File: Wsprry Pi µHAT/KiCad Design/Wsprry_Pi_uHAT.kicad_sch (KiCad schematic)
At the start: 9 parts, among them J1 GPIO, SW1 SW_Push, U2 CAT24C32

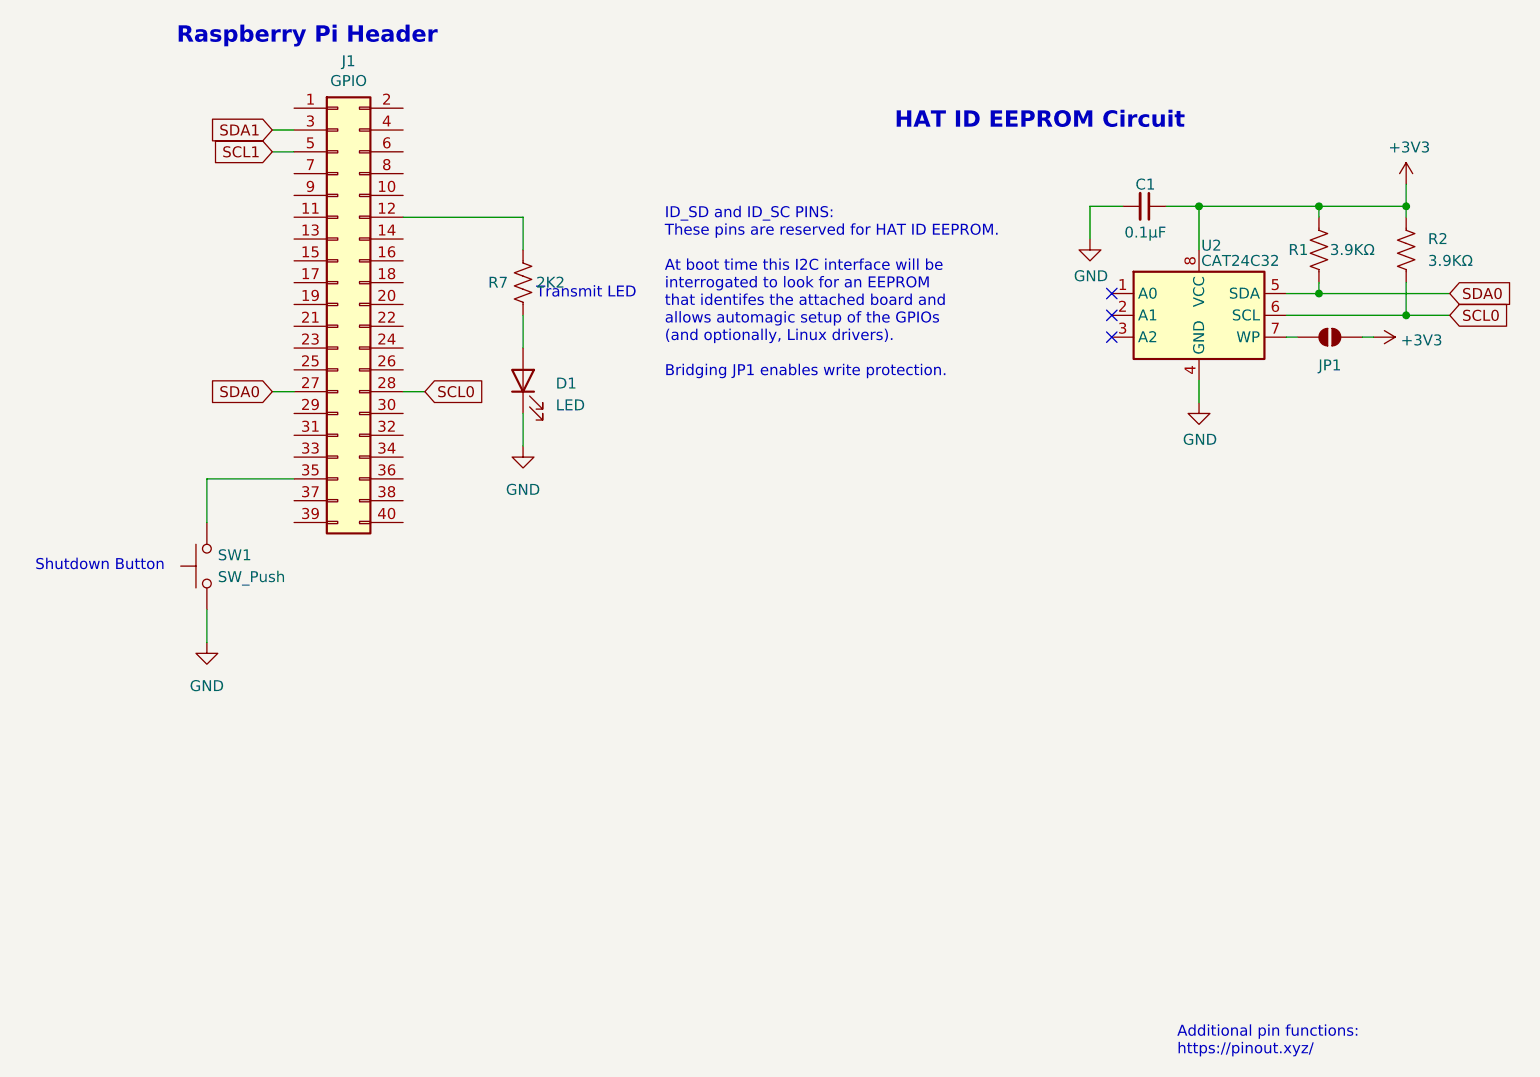
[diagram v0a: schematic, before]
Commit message: Set up hierarchical sheets
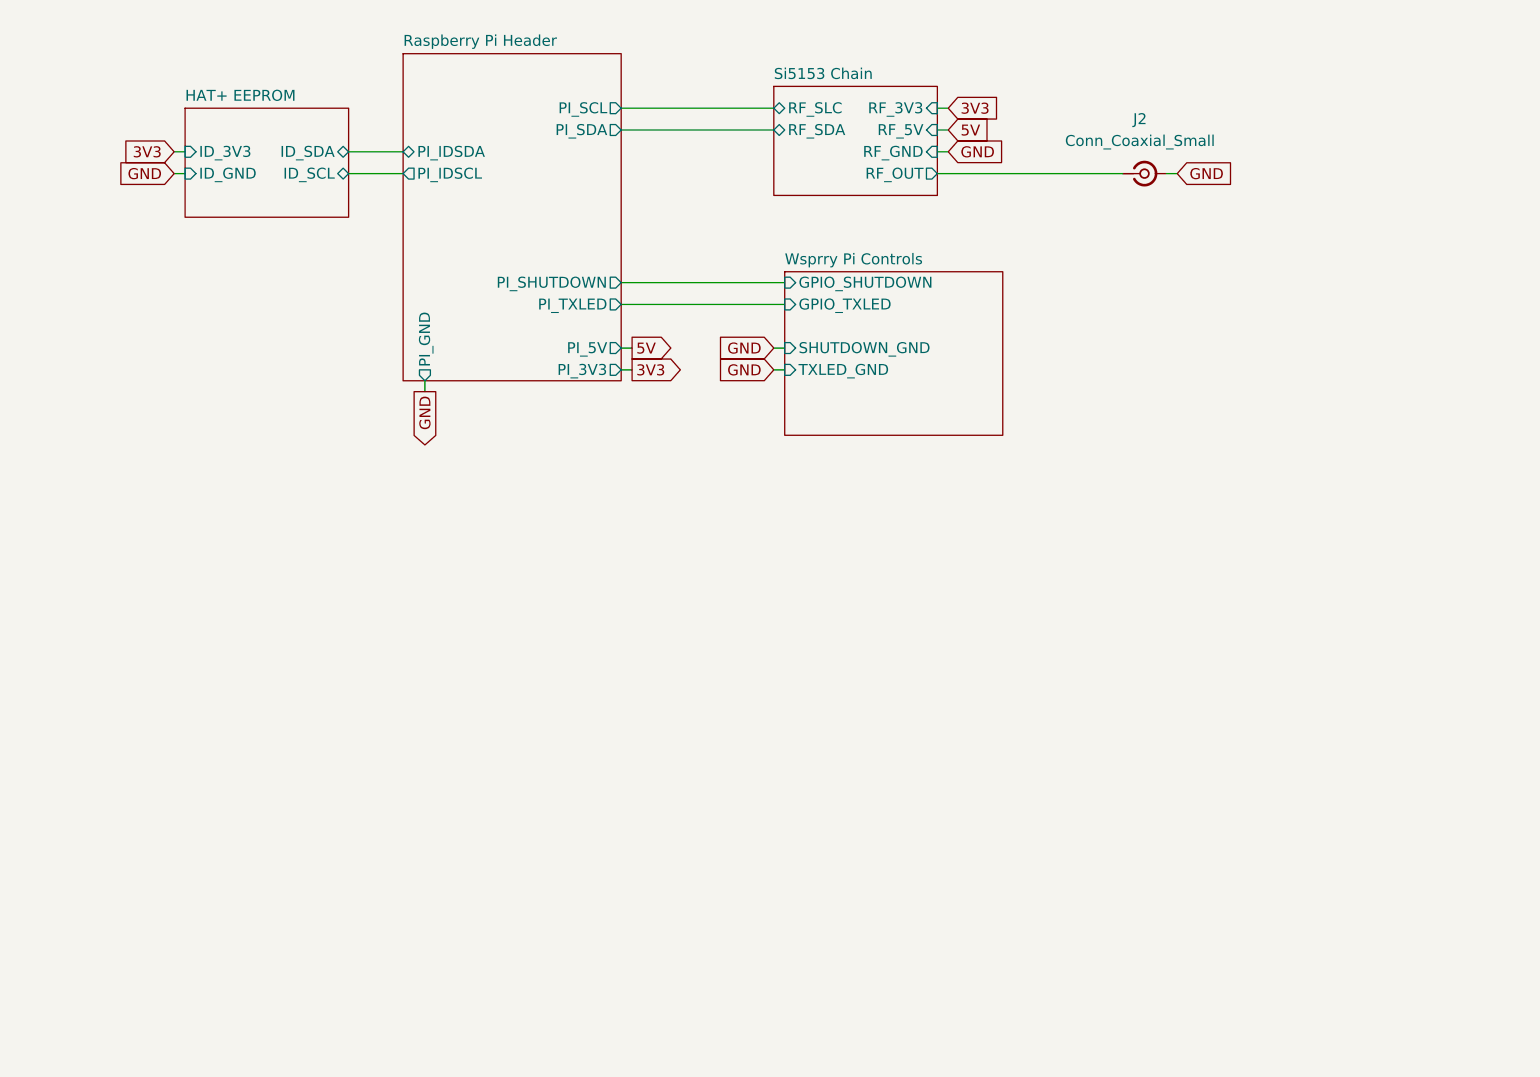
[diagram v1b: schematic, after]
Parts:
- removed C1: 0.1µF, Capacitor_SMD:C_0201_0603Metric, symbol Device:C_Small
- removed D1: LED, symbol Device:LED
- removed J1: GPIO, Connector_PinSocket_2.54mm:PinSocket_2x20_P2.54mm_Vertical, symbol Connector_Generic:Conn_02x20_Odd_Even
- removed JP1: ID_WP, Jumper:SolderJumper-2_P1.3mm_Open_RoundedPad1.0x1.5mm, symbol Jumper:SolderJumper_2_Open
- removed R1, R2: 3.9KΩ, Resistor_SMD:R_0201_0603Metric, symbol Device:R_US
- removed R7: 2K2, symbol Device:R_US
- removed SW1: SW_Push, symbol Switch:SW_Push
- removed U2: CAT24C32, Package_SO:TSSOP-8_4.4x3mm_P0.65mm, symbol Memory_EEPROM:CAT24C128
- added J2: Conn_Coaxial_Small, symbol Connector:Conn_Coaxial_Small
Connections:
- net GND: now also J2.2 (Ext)
- new net Si5153 Chain/RF_OUT: J2.1 (In)
- no-connect marks 3 -> 0
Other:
- added sheet HAT+ EEPROM (../../Raspberry Pi HAT EEPROM/KiCad Design/id_eeprom.kicad_sch)
- added sheet Raspberry Pi Header (../../Raspberry Pi Header/KiCad Design/Raspberry Pi Header.kicad_sch)
- added sheet Si5153 Chain (../../WSPR Si5153 RF Chain/KiCad Design/WSPR Si5351 RF Chain.kicad_sch)
- added sheet Wsprry Pi Controls (../../Wsprry Pi Controls/KiCad Design/Wsprry Pi Controls.kicad_sch)
- note removed: "Additional pin functions: https://pinout.xyz/"
- note removed: "HAT ID EEPROM Circuit"
- note removed: "ID_SD and ID_SC PINS: These pins are reserved for HAT ID EEPROM. At boot time this I2C interface will be interrogated to look for an EEPROM that identifes the attached board and allows automagic setup of the GPIOs (and optionally, Linux drivers). Bridging JP1 enables write protection."
- note removed: "Raspberry Pi Header"
- note removed: "Shutdown Button"
- note removed: "Transmit LED"

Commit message: Notionally complete through PA
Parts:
- removed J2: Conn_Coaxial_Small, symbol Connector:Conn_Coaxial_Small
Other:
- sheet HAT+ EEPROM: file ../../Raspberry Pi HAT EEPROM/KiCad Design/id_eeprom.kicad_sch -> ../../Raspberry Pi HAT EEPROM/KiCad Design/Raspberry Pi HAT EEPROM.kicad_sch
- sheet Wsprry Pi Controls ports: added SHUTDOWN_3V3; removed none
